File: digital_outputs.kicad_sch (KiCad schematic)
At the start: 82 parts, among them Q601 BC817, Q602 BC817, Q603 BC817, Q604 BC817, Q605 BC817, Q606 BC817, Q607 BC817, Q608 BC817, Q609 BC807, Q610 BC807, Q611 BC807, Q612 BC807, Q613 BC817, Q614 BC817, Q615 BC817, Q616 BC817, Q617 BC817, Q618 BC817, Q619 BC817, Q620 BC817, Q621 BC807, Q622 BC807, Q623 BC807, Q624 BC807

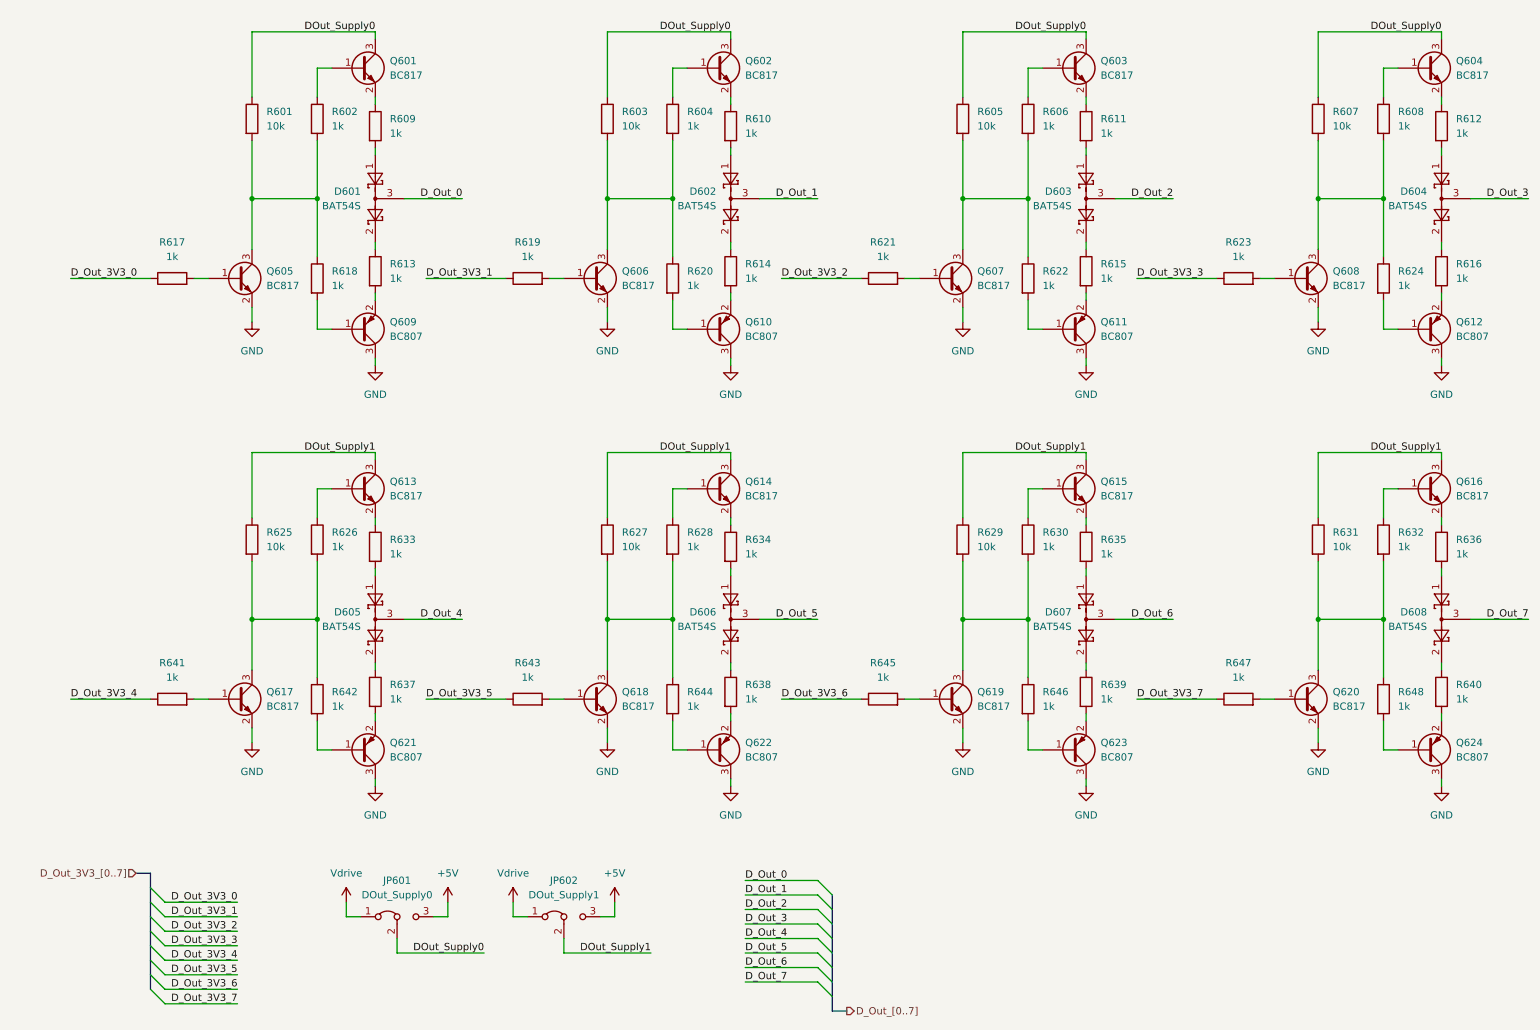
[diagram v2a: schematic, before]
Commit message: hierarchical sheets for digital I/O and replaced power supply jumpers with relays
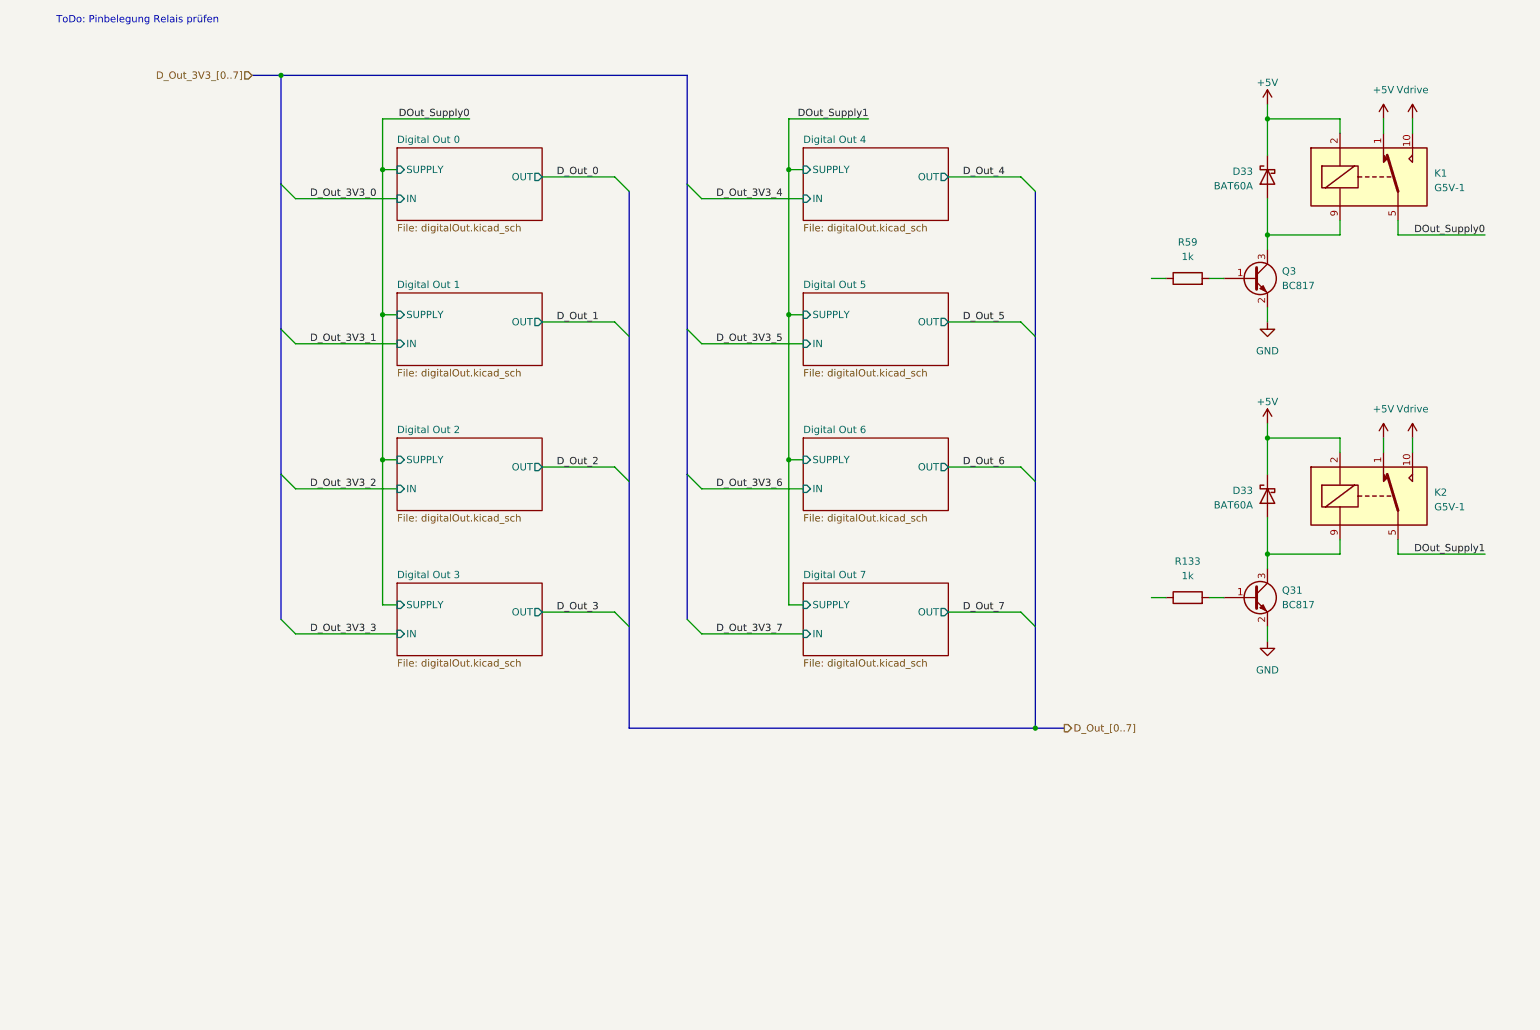
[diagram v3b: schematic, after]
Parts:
- removed D601, D602, D603, D604, D605, D606, D607, D608: BAT54S, Package_TO_SOT_SMD:SOT-23, symbol FaSTTUBe_PnP:BAT54S
- removed JP601: DOut_Supply0, Connector_PinHeader_2.54mm:PinHeader_1x03_P2.54mm_Vertical, symbol Jumper:Jumper_3_Bridged12
- removed JP602: DOut_Supply1, Connector_PinHeader_2.54mm:PinHeader_1x03_P2.54mm_Vertical, symbol Jumper:Jumper_3_Bridged12
- removed Q601, Q602, Q603, Q604, Q605, Q606, Q607, Q608, Q613, Q614, Q615, Q616, Q617, Q618, Q619, Q620: BC817, Package_TO_SOT_SMD:SOT-23, symbol FaSTTUBe_PnP:BC817
- removed Q609, Q610, Q611, Q612, Q621, Q622, Q623, Q624: BC807, Package_TO_SOT_SMD:SOT-23, symbol FaSTTUBe_PnP:BC807
- removed R601, R603, R605, R607, R625, R627, R629, R631: 10k, Resistor_SMD:R_0603_1608Metric, symbol Device:R
- removed R602, R604, R606, R608, R609, R610, R611, R612, R613, R614, R615, R616, R617, R618, R619, R620, R621, R622, R623, R624, R626, R628, R630, R632, R633, R634, R635, R636, R637, R638, R639, R640, R641, R642, R643, R644, R645, R646, R647, R648: 1k, Resistor_SMD:R_0603_1608Metric, symbol Device:R
- added D33 (x2): BAT60A, Diode_SMD:D_SOD-323, symbol Diode:BAT60A
- added K1, K2: G5V-1, Relay_THT:Relay_SPDT_Omron_G5V-1, symbol Relay:G5V-1
- added Q3, Q31: BC817, Package_TO_SOT_SMD:SOT-23, symbol FaSTTUBe_PnP:BC817
- added R133, R59: 1k, Resistor_SMD:R_0603_1608Metric, symbol Device:R
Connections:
- net +5V: now also D33.1 (K), D33.1 (K), K1.1, K1.2, K2.1, K2.2
- net DOut_Supply0: now also K1.5, K1.6
- net DOut_Supply1: now also K2.5, K2.6
- net GND: now also Q3.2 (E), Q31.2 (E)
- net Vdrive: now also K1.10, K2.10
- new net: Q3.1 (B), R59.2
- new net: D33.2 (A), K1.9, Q3.3 (C)
- new net: Q31.1 (B), R133.2
- new net: D33.2 (A), K2.9, Q31.3 (C)
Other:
- added sheet Digital Out 0 (digitalOut.kicad_sch)
- added sheet Digital Out 1 (digitalOut.kicad_sch)
- added sheet Digital Out 2 (digitalOut.kicad_sch)
- added sheet Digital Out 3 (digitalOut.kicad_sch)
- added sheet Digital Out 4 (digitalOut.kicad_sch)
- added sheet Digital Out 5 (digitalOut.kicad_sch)
- added sheet Digital Out 6 (digitalOut.kicad_sch)
- added sheet Digital Out 7 (digitalOut.kicad_sch)
- note added: "ToDo: Pinbelegung Relais prüfen"
